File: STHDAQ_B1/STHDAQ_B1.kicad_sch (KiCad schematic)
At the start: 3 parts, among them J1 532611071, U1 IP5306, U2 102010448

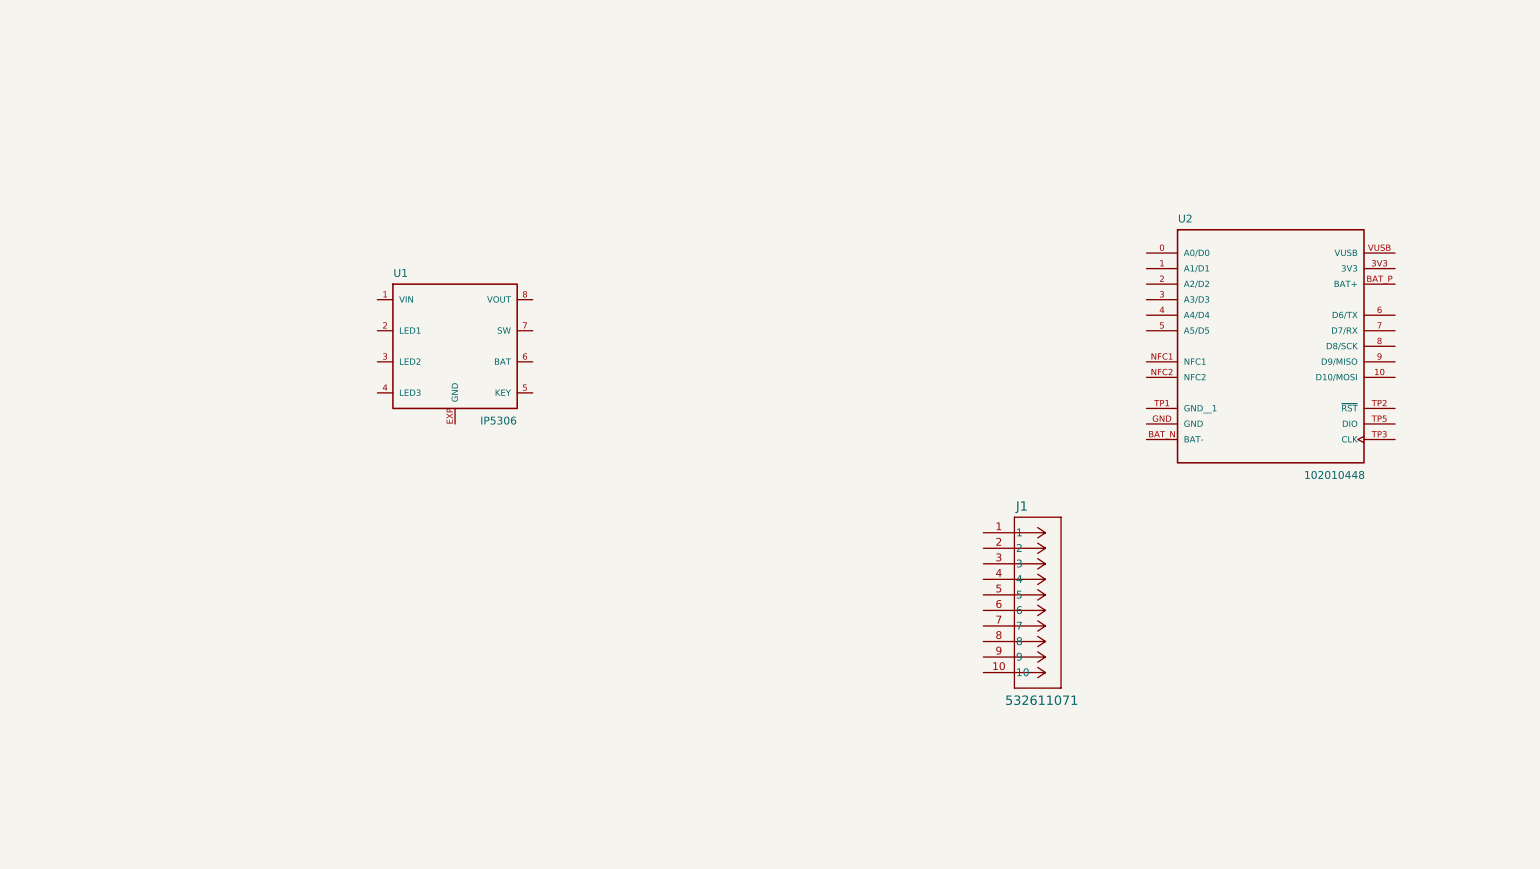
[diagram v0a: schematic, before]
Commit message: B1 schematic ~80% completion
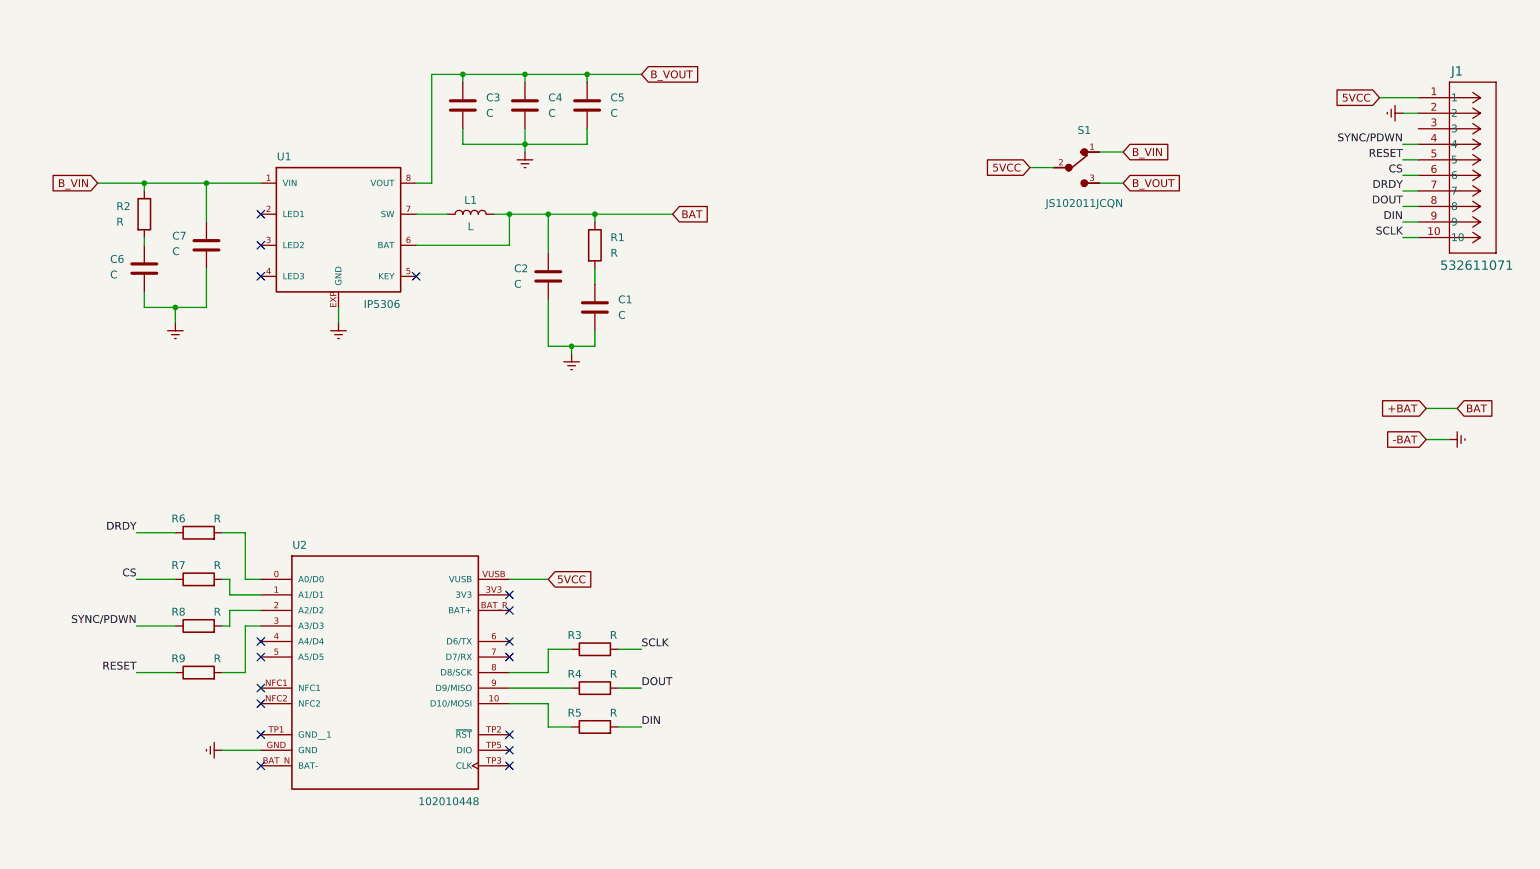
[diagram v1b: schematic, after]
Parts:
- added C1, C2, C3, C4, C5, C6, C7: C, symbol Device:C
- added L1: L, symbol Device:L
- added R1, R2, R3, R4, R5, R6, R7, R8, R9: R, symbol Device:R
- added S1: JS102011JCQN, daFootprints:SW_JS102011JCQN, symbol SW_JS102011JCQN:JS102011JCQN
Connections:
- net B_VIN: now reaches U1.1 (VIN)
- net B_VIN: now also C7.1, R2.1, S1.1
- net +BAT: now reaches U1.6 (BAT)
- net +BAT: now also C2.1, L1.2, R1.1
- net at U1.7 (SW): now also L1.1
- net B_VOUT: now reaches U1.8 (VOUT)
- net B_VOUT: now also C3.1, C4.1, C5.1, S1.3
- net Earth: now reaches U1.EXP (GND)
- net Earth: now also J1.2, U2.GND, C1.2, C2.2, C3.2, C4.2, C5.2, C6.2, C7.2
- net at U2.0 (A0/D0): now also R6.2
- net at U2.1 (A1/D1): now also R7.2
- net at U2.10 (D10/MOSI): now also R5.1
- net at U2.2 (A2/D2): now also R8.2
- net at U2.3 (A3/D3): now also R9.2
- net at U2.8 (D8/SCK): now also R3.1
- net at U2.9 (D9/MISO): now also R4.1
- net 5VCC: now reaches U2.VUSB
- net 5VCC: now also J1.1, S1.2
- net SCLK: now reaches J1.10
- net SCLK: now also R3.2
- net SYNC/PDWN: now reaches J1.4
- net SYNC/PDWN: now also R8.1
- net RESET: now reaches J1.5
- net RESET: now also R9.1
- net CS: now reaches J1.6
- net CS: now also R7.1
- net DRDY: now reaches J1.7
- net DRDY: now also R6.1
- net DOUT: now reaches J1.8
- net DOUT: now also R4.2
- net DIN: now reaches J1.9
- net DIN: now also R5.2
- new net: C1.1, R1.2
- new net: C6.1, R2.2
- no-connect marks 0 -> 17
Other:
- moved on the sheet: J1, U1, U2

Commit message: prettify B1
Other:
- note added: "Battery terminals"
- note added: "Charge/Discharge switch"
- note added: "Connector for signal conditioning module"
- note added: "IP5306 Charge Discharge Module"
- note added: "nrf52840 Microcontroller"
- moved on the sheet: C1, C2, C3, C4, C5, C6, C7, J1, L1, R1, R2, R3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

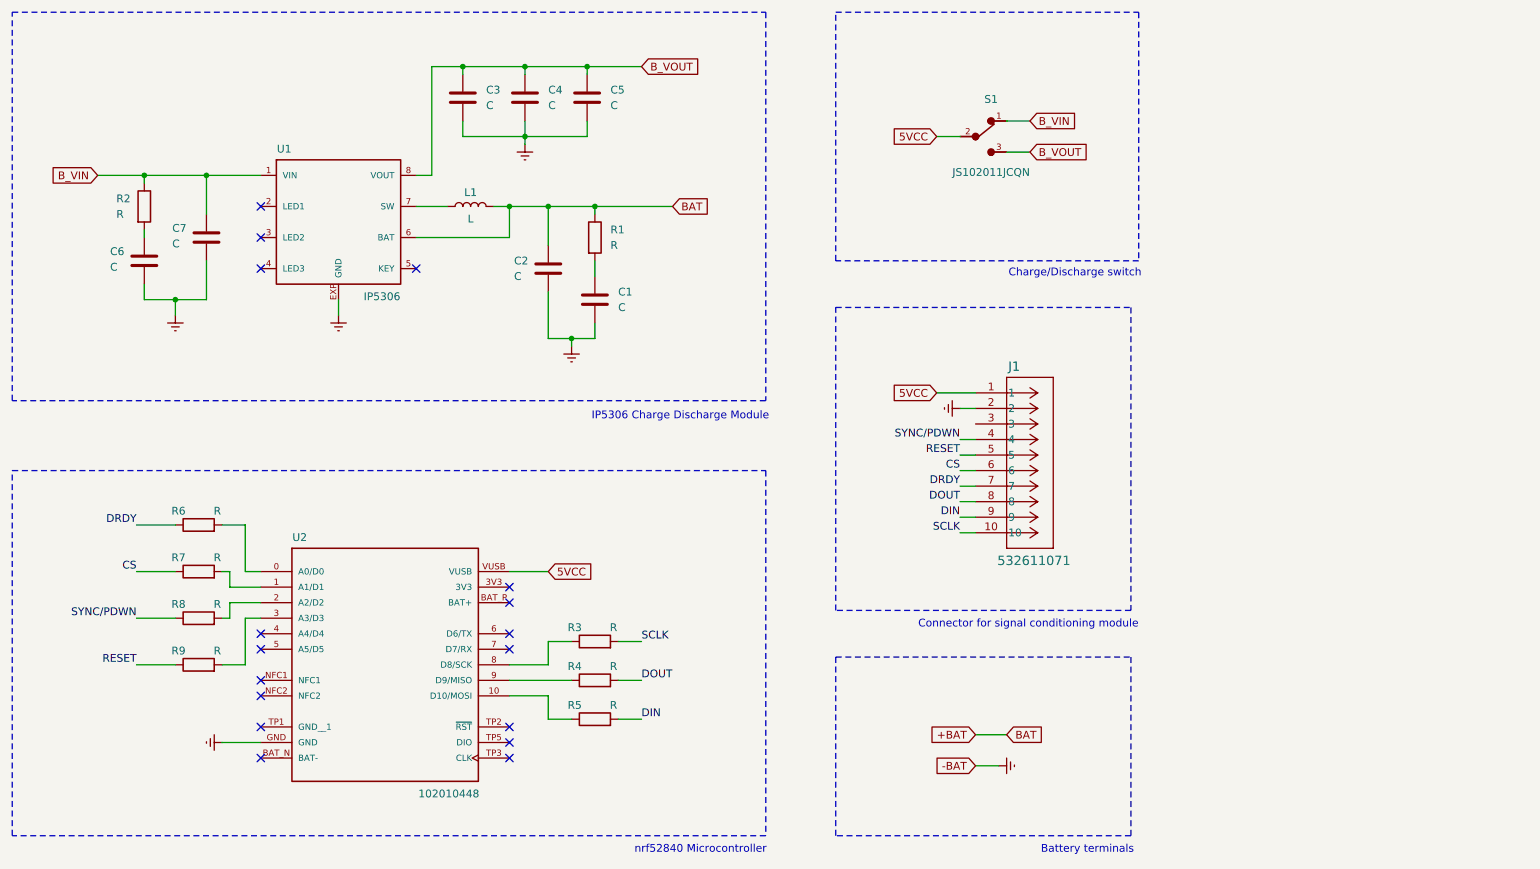
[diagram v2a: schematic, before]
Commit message: added resistance values for B0
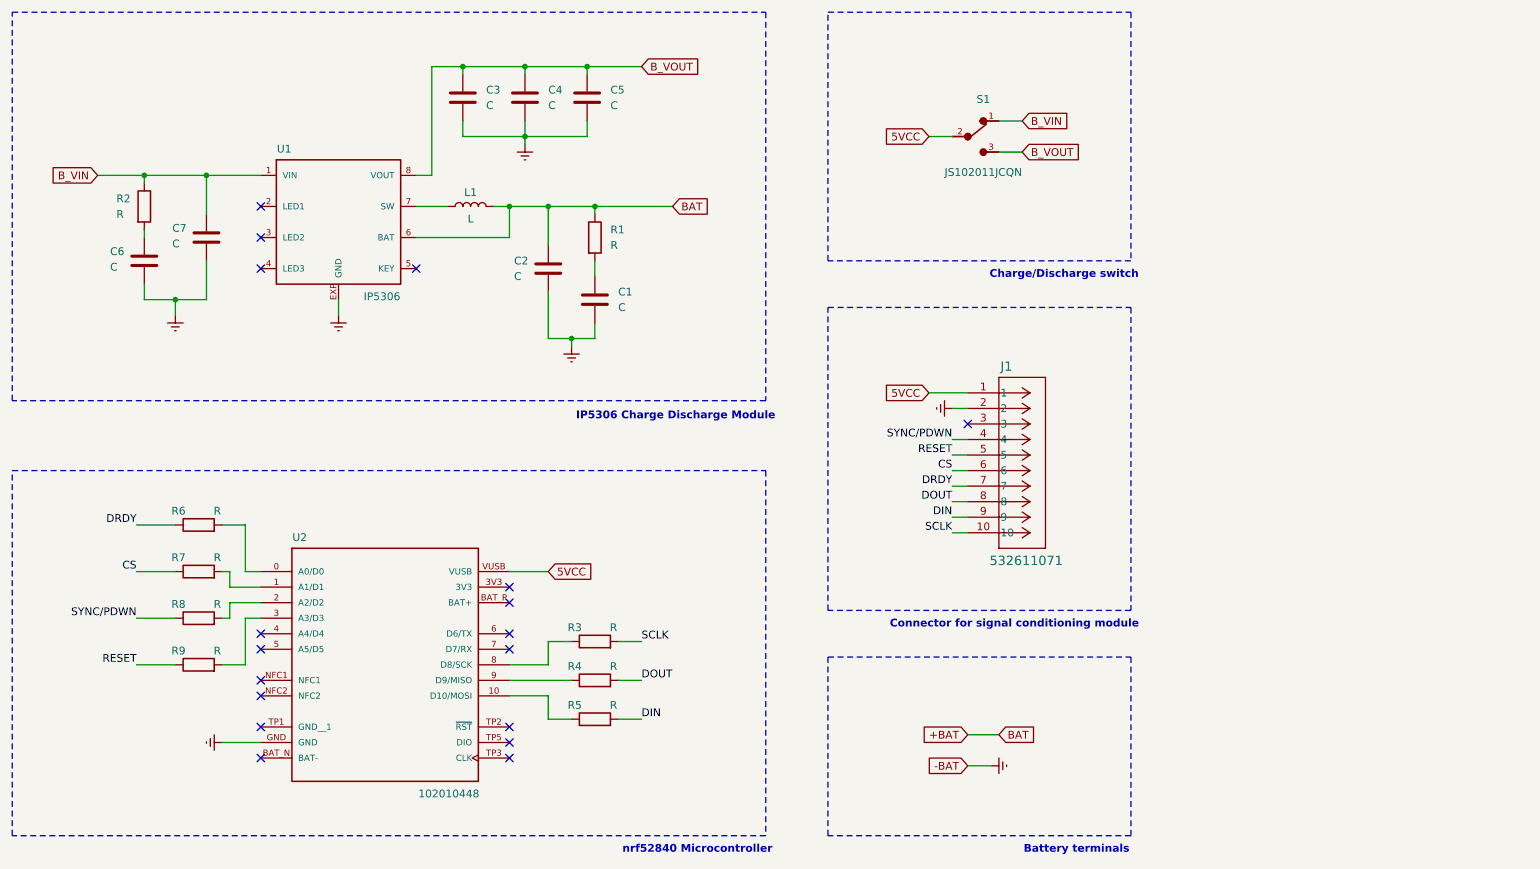
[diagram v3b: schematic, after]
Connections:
- no-connect marks 17 -> 18
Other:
- moved on the sheet: J1, S1

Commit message: B1 pcb layouting
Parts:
- added D1: 25%, LED_SMD:LED_0201_0603Metric, symbol Device:LED
- added D2: 50%, LED_SMD:LED_0201_0603Metric, symbol Device:LED
- added D3: 75%, LED_SMD:LED_0201_0603Metric, symbol Device:LED
- added D4: 100%, LED_SMD:LED_0201_0603Metric, symbol Device:LED
- added D5: LED, LED_SMD:LED_0201_0603Metric, symbol Device:LED
- added H1, H2, H3, H4: MountingHole, MountingHole:MountingHole_3.2mm_M3_ISO14580_Pad_TopBottom, symbol Mechanical:MountingHole
- added P1, P2: S2B-PH-SM4-TB, daFootprintsBX:JST_S2B-PH-SM4-TB, symbol JST_S2B-PH-SM4-TB:S2B-PH-SM4-TB
- added R6, R7: 10K, Resistor_SMD:R_0201_0603Metric, symbol Device:R
- added SW1: SW_Push, Button_Switch_SMD:Panasonic_EVQPUJ_EVQPUA, symbol Switch:SW_Push
- C1: renamed from C6; value C -> 10u; footprint (none) -> Capacitor_SMD:C_0201_0603Metric
- C2: renamed from C7; value C -> 10u; footprint (none) -> Capacitor_SMD:C_0201_0603Metric
- C3, C4: value C -> 22u; footprint (none) -> Capacitor_SMD:C_0201_0603Metric
- C5: renamed from C2; value C -> 10u; footprint (none) -> Capacitor_SMD:C_0201_0603Metric
- C6: renamed from C5; value C -> 22u; footprint (none) -> Capacitor_SMD:C_0201_0603Metric
- C7: renamed from C1; value C -> 10u; footprint (none) -> Capacitor_SMD:C_0201_0603Metric
- L1: value L -> 1uH; footprint (none) -> Inductor_SMD:L_0201_0603Metric
- R1: renamed from R2; value R -> 10K; footprint (none) -> Resistor_SMD:R_0201_0603Metric
- R10: renamed from R4; value R -> 100; footprint (none) -> Resistor_SMD:R_0201_0603Metric
- R11: renamed from R5; value R -> 100; footprint (none) -> Resistor_SMD:R_0201_0603Metric
- R2: renamed from R6; value R -> 100; footprint (none) -> Resistor_SMD:R_0201_0603Metric
- R3: renamed from R7; value R -> 100; footprint (none) -> Resistor_SMD:R_0201_0603Metric
- R4: renamed from R8; value R -> 100; footprint (none) -> Resistor_SMD:R_0201_0603Metric
- R5: renamed from R9; value R -> 100; footprint (none) -> Resistor_SMD:R_0201_0603Metric
- R8: renamed from R1; value R -> 10K; footprint (none) -> Resistor_SMD:R_0201_0603Metric
- R9: renamed from R3; value R -> 100; footprint (none) -> Resistor_SMD:R_0201_0603Metric
- S1: footprint daFootprints:SW_JS102011JCQN -> daFootprintsB1:SW_JS102011JCQN
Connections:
- net Earth: now also D5.1 (K), P1.2, P2.2, SW1.2
- net at U1.2 (LED1): now also D1.2 (A), D2.1 (K)
- net at U1.3 (LED2): now also D3.2 (A), D4.1 (K)
- net at U1.4 (LED3): now also D1.1 (K), D2.2 (A), D3.1 (K), D4.2 (A)
- net at U1.5 (KEY): now also R6.1, R7.1
- net +BAT renamed BAT
- net BAT: now also P1.1, P2.1
- new net: D5.2 (A), R6.2
- new net: R7.2, SW1.1
- no-connect marks 18 -> 14
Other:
- moved on the sheet: C1, C2, J1, R1

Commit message: B1 pcb layouting
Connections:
- net 5VCC: now also J1.10; no longer J1.1
- net CS: now also J1.5; no longer J1.6
- net DIN: now also J1.2; no longer J1.9
- net DOUT: now also J1.3; no longer J1.8
- net DRDY: now also J1.4; no longer J1.7
- net Earth: now also J1.9; no longer J1.2
- net RESET: now also J1.6; no longer J1.5
- net SCLK: now also J1.1; no longer J1.10
- net SYNC/PDWN: now also J1.7; no longer J1.4
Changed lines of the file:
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@@
-	)
-	(no_connect
-		(at 176.53 82.55)
 	)
 	(no_connect
@@
 	)
 	(no_connect
+		(at 176.53 95.25)
+	)
+	(no_connect
 		(at 101.6 135.89)
 	)
@@
 	(wire
 		(pts
+			(xy 171.45 101.6) (xy 176.53 101.6)
+		)
+		(stroke
+			(width 0)
+			(type default)
+		)
+	)
+	(wire
+		(pts
 			(xy 34.29 24.13) (xy 34.29 22.86)
 		)
@@
 	(wire
 		(pts
-			(xy 173.99 85.09) (xy 176.53 85.09)
-		)
-		(stroke
-			(width 0)
-			(type default)
-		)
-	)
-	(wire
-		(pts
 			(xy 111.76 72.39) (xy 111.76 73.66)
 		)
@@
 	(wire
 		(pts
+			(xy 165.1 77.47) (xy 176.53 77.47)
+		)
+		(stroke
+			(width 0)
+			(type default)
+		)
+	)
+	(wire
+		(pts
 			(xy 55.88 110.49) (xy 55.88 113.03)
 		)
@@
 	(wire
 		(pts
+			(xy 165.1 80.01) (xy 176.53 80.01)
+		)
+		(stroke
+			(width 0)
+			(type default)
+		)
+	)
+	(wire
+		(pts
 			(xy 54.61 125.73) (xy 58.42 125.73)
 		)
@@
 	(wire
 		(pts
+			(xy 165.1 87.63) (xy 176.53 87.63)
+		)
+		(stroke
+			(width 0)
+			(type default)
+		)
+	)
+	(wire
+		(pts
 			(xy 170.18 39.37) (xy 173.99 39.37)
 		)
@@
 	(wire
 		(pts
+			(xy 165.1 90.17) (xy 176.53 90.17)
+		)
+		(stroke
+			(width 0)
+			(type default)
+		)
+	)
+	(wire
+		(pts
 			(xy 57.15 60.96) (xy 57.15 73.66)
 		)
@@
 	(wire
 		(pts
+			(xy 165.1 92.71) (xy 176.53 92.71)
+		)
+		(stroke
+			(width 0)
+			(type default)
+		)
+	)
+	(wire
+		(pts
 			(xy 54.61 102.87) (xy 58.42 102.87)
 		)
@@
 	(wire
 		(pts
-			(xy 173.99 92.71) (xy 176.53 92.71)
-		)
-		(stroke
-			(width 0)
-			(type default)
-		)
-	)
-	(wire
-		(pts
 			(xy 93.98 29.21) (xy 93.98 27.94)
 		)
@@
 	(wire
 		(pts
-			(xy 173.99 80.01) (xy 176.53 80.01)
-		)
-		(stroke
-			(width 0)
-			(type default)
-		)
-	)
-	(wire
-		(pts
 			(xy 93.98 27.94) (xy 88.9 27.94)
 		)
@@
 	(wire
 		(pts
-			(xy 170.18 77.47) (xy 176.53 77.47)
-		)
-		(stroke
-			(width 0)
-			(type default)
-		)
-	)
-	(wire
-		(pts
 			(xy 107.95 110.49) (xy 101.6 110.49)
 		)
@@
 	(wire
 		(pts
+			(xy 165.1 85.09) (xy 176.53 85.09)
+		)
+		(stroke
+			(width 0)
+			(type default)
+		)
+	)
+	(wire
+		(pts
 			(xy 107.95 57.15) (xy 107.95 50.8)
 		)
@@
 	(wire
 		(pts
-			(xy 173.99 87.63) (xy 176.53 87.63)
-		)
-		(stroke
-			(width 0)
-			(type default)
-		)
-	)
-	(wire
-		(pts
 			(xy 34.29 43.18) (xy 39.37 43.18)
 		)
@@
 	(wire
 		(pts
+			(xy 166.37 97.79) (xy 176.53 97.79)
+		)
+		(stroke
+			(width 0)
+			(type default)
+		)
+	)
+	(wire
+		(pts
 			(xy 104.14 27.94) (xy 93.98 27.94)
 		)
@@
 	(wire
 		(pts
-			(xy 173.99 95.25) (xy 176.53 95.25)
-		)
-		(stroke
-			(width 0)
-			(type default)
-		)
-	)
-	(wire
-		(pts
-			(xy 173.99 100.33) (xy 176.53 100.33)
-		)
-		(stroke
-			(width 0)
-			(type default)
-		)
-	)
-	(wire
-		(pts
 			(xy 99.06 50.8) (xy 101.6 50.8)
 		)
@@
 	(wire
 		(pts
-			(xy 173.99 97.79) (xy 176.53 97.79)
+			(xy 165.1 82.55) (xy 176.53 82.55)
 		)
 		(stroke
@@
 	(wire
 		(pts
-			(xy 173.99 90.17) (xy 176.53 90.17)
-		)
-		(stroke
-			(width 0)
-			(type default)
-		)
-	)
-	(wire
-		(pts
 			(xy 44.45 43.18) (xy 39.37 43.18)
 		)
@@
 		(pts
 			(xy 40.64 102.87) (xy 46.99 102.87)
+		)
+		(stroke
+			(width 0)
+			(type default)
+		)
+	)
+	(wire
+		(pts
+			(xy 176.53 101.6) (xy 176.53 100.33)
 		)
 		(stroke
@@
 	)
 	(label "CS"
-		(at 173.99 90.17 180)
-		(fields_autoplaced yes)
-		(effects
-			(font
-				(size 1.27 1.27)
-			)
-			(justify right bottom)
+		(at 165.1 87.63 0)
+		(fields_autoplaced yes)
+		(effects
+			(font
+				(size 1.27 1.27)
+			)
+			(justify left bottom)
 		)
 	)
@@
 	)
 	(label "DIN"
-		(at 173.99 97.79 180)
-		(fields_autoplaced yes)
-		(effects
-			(font
-				(size 1.27 1.27)
-			)
-			(justify right bottom)
+		(at 165.1 80.01 0)
+		(fields_autoplaced yes)
+		(effects
+			(font
+				(size 1.27 1.27)
+			)
+			(justify left bottom)
 		)
 	)
@@
 	)
 	(label "SYNC{slash}PDWN"
-		(at 173.99 85.09 180)
-		(fields_autoplaced yes)
-		(effects
-			(font
-				(size 1.27 1.27)
-			)
-			(justify right bottom)
+		(at 165.1 92.71 0)
+		(fields_autoplaced yes)
+		(effects
+			(font
+				(size 1.27 1.27)
+			)
+			(justify left bottom)
 		)
 	)
@@
 	)
 	(label "DOUT"
-		(at 173.99 95.25 180)
-		(fields_autoplaced yes)
-		(effects
-			(font
-				(size 1.27 1.27)
-			)
-			(justify right bottom)
+		(at 165.1 82.55 0)
+		(fields_autoplaced yes)
+		(effects
+			(font
+				(size 1.27 1.27)
+			)
+			(justify left bottom)
 		)
 	)
 	(label "RESET"
-		(at 173.99 87.63 180)
-		(fields_autoplaced yes)
-		(effects
-			(font
-				(size 1.27 1.27)
-			)
-			(justify right bottom)
+		(at 165.1 90.17 0)
+		(fields_autoplaced yes)
+		(effects
+			(font
+				(size 1.27 1.27)
+			)
+			(justify left bottom)
 		)
 	)
 	(label "SCLK"
-		(at 173.99 100.33 180)
-		(fields_autoplaced yes)
-		(effects
-			(font
-				(size 1.27 1.27)
-			)
-			(justify right bottom)
+		(at 165.1 77.47 0)
+		(fields_autoplaced yes)
+		(effects
+			(font
+				(size 1.27 1.27)
+			)
+			(justify left bottom)
 		)
 	)
@@
 	)
 	(label "DRDY"
-		(at 173.99 92.71 180)
-		(fields_autoplaced yes)
-		(effects
-			(font
-				(size 1.27 1.27)
-			)
-			(justify right bottom)
+		(at 165.1 85.09 0)
+		(fields_autoplaced yes)
+		(effects
+			(font
+				(size 1.27 1.27)
+			)
+			(justify left bottom)
 		)
 	)
@@
 	(global_label "5VCC"
 		(shape input)
-		(at 170.18 77.47 180)
+		(at 171.45 101.6 180)
 		(fields_autoplaced yes)
 		(effects
@@
 		)
 		(property "Intersheetrefs" "${INTERSHEET_REFS}"
-			(at 162.6093 77.47 0)
+			(at 163.6267 101.6 0)
 			(effects
 				(font
@@
 	(symbol
 		(lib_id "power:Earth")
-		(at 173.99 80.01 270)
+		(at 166.37 97.79 270)
 		(unit 1)
 		(exclude_from_sim no)
@@
 		(fields_autoplaced yes)
 		(property "Reference" "#PWR07"
-			(at 167.64 80.01 0)
+			(at 160.02 97.79 0)
 			(effects
 				(font
@@
 		)
 		(property "Value" "Earth"
-			(at 170.18 80.01 90)
+			(at 162.56 97.79 90)
 			(effects
 				(font
@@
 		)
 		(property "Footprint" ""
-			(at 173.99 80.01 0)
+			(at 166.37 97.79 0)
 			(effects
 				(font
@@
 		)
 		(property "Datasheet" "~"
-			(at 173.99 80.01 0)
+			(at 166.37 97.79 0)
 			(effects
 				(font
@@
 		)
 		(property "Description" "Power symbol creates a global label with name \"Earth\""
-			(at 173.99 80.01 0)
-			(effects
-				(font
+			(at 166.37 97.79 0)
+			(effects
+				(font
